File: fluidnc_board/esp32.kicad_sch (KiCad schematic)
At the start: 30 parts

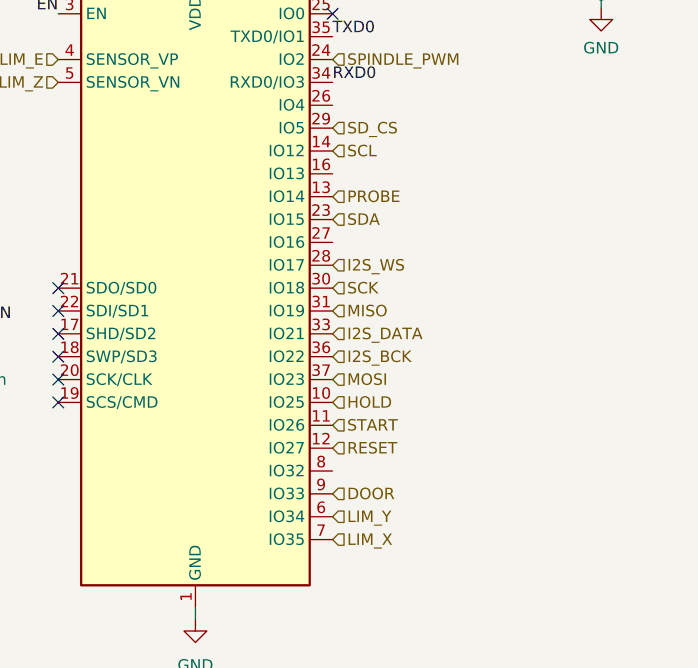
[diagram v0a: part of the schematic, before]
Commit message: outputs, spindle output and switch inputs
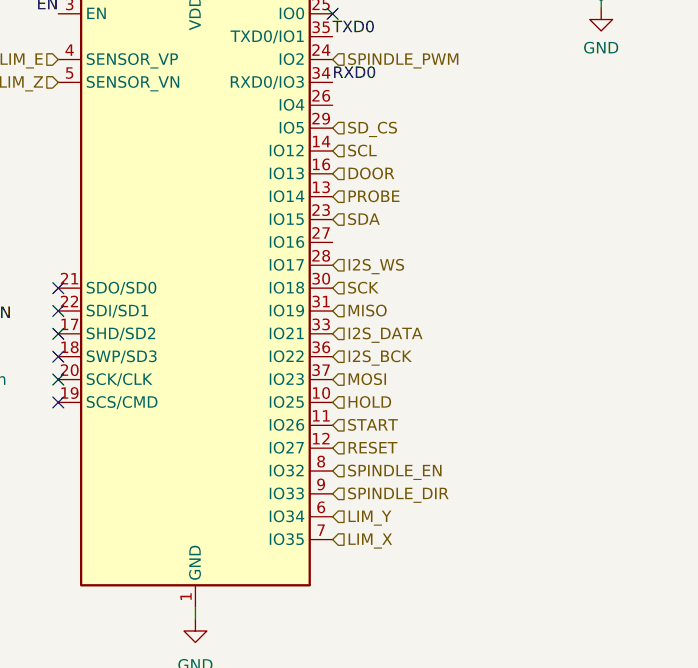
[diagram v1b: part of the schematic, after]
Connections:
- net DOOR: now also U?.16 (IO13); no longer U?.9 (IO33)
- net SPINDLE_EN: now reaches U?.8 (IO32)
- new net SPINDLE_DIR: U?.9 (IO33)
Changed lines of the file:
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@@
     (effects (font (size 1.27 1.27)) (justify left))
   )
-  (hierarchical_label "DOOR" (shape input) (at 222.25 101.6 0)
+  (hierarchical_label "DOOR" (shape input) (at 222.25 66.04 0)
     (effects (font (size 1.27 1.27)) (justify left))
   )
@@
     (effects (font (size 1.27 1.27)) (justify left))
   )
+  (hierarchical_label "SPINDLE_DIR" (shape input) (at 222.25 101.6 0)
+    (effects (font (size 1.27 1.27)) (justify left))
+  )
   (hierarchical_label "I2S_WS" (shape input) (at 222.25 76.2 0)
     (effects (font (size 1.27 1.27)) (justify left))
@@
     (effects (font (size 1.27 1.27)) (justify left))
   )
+  (hierarchical_label "SPINDLE_EN" (shape input) (at 222.25 99.06 0)
+    (effects (font (size 1.27 1.27)) (justify left))
+  )

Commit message: remove unnecessary i2s chip
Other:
- title: (none) -> ESP32 MCU
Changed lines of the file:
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@@
 (kicad_sch (version 20211123) (generator eeschema)
   (paper "A4")
+  (title_block
+    (title "ESP32 MCU")
+  )
   (junction (at 201.93 150.495) (diameter 0) (color 0 0 0 0)
   )

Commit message: footprint associations and part no.
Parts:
- C56, C58, C62: renamed from C?; footprint (none) -> Capacitor_SMD:C_0603_1608Metric_Pad1.05x0.95mm_HandSolder; Digikey Part No. (none) -> 1276-1941-1-ND
- C57: renamed from C?; footprint (none) -> Capacitor_SMD:C_0805_2012Metric_Pad1.18x1.45mm_HandSolder; Digikey Part No. (none) -> 1276-1248-1-ND
- C59, C60: renamed from C?; value C -> 100n; footprint (none) -> Capacitor_SMD:C_0603_1608Metric_Pad1.05x0.95mm_HandSolder; Digikey Part No. (none) -> 1276-1941-1-ND
- C61: renamed from C?; value 22u -> 4.7u; footprint (none) -> Capacitor_SMD:C_0805_2012Metric_Pad1.18x1.45mm_HandSolder; Digikey Part No. (none) -> 1276-1248-1-ND
- D42, D43, D44: renamed from D?; Digikey Part No. (none) -> ESD5V0D5-TPMSCT-ND
- D45, D46: renamed from D?; footprint (none) -> LED_SMD:LED_1206_3216Metric_Pad1.42x1.75mm_HandSolder; Digikey Part No. (none) -> 160-1456-1-ND
- J19: renamed from J?; footprint (none) -> Connector_USB:USB_B_OST_USB-B1HSxx_Horizontal
- Q5, Q6: renamed from Q?; Digikey Part No. (none) -> 641-1790-1-ND
- R39, R40: renamed from R?; footprint (none) -> Resistor_SMD:R_1206_3216Metric_Pad1.30x1.75mm_HandSolder; Digikey Part No. (none) -> 311-0.0ERCT-ND
- R41, R42, R49: renamed from R?; footprint (none) -> Resistor_SMD:R_0805_2012Metric_Pad1.20x1.40mm_HandSolder; Digikey Part No. (none) -> 311-10KARCT-ND
- R43, R47: renamed from R?; footprint (none) -> Resistor_SMD:R_0603_1608Metric_Pad0.98x0.95mm_HandSolder; Digikey Part No. (none) -> 311-100GRCT-ND
- R44: renamed from R?; footprint (none) -> Resistor_SMD:R_0201_0603Metric_Pad0.64x0.40mm_HandSolder; Digikey Part No. (none) -> 311-22.0KHRCT-ND
- R45: renamed from R?; footprint (none) -> Resistor_SMD:R_0805_2012Metric_Pad1.15x1.40mm_HandSolder; Digikey Part No. (none) -> 311-47KARCT-ND
- R46: renamed from R?; value R -> 2.2k; footprint (none) -> Resistor_SMD:R_0603_1608Metric_Pad0.98x0.95mm_HandSolder; Digikey Part No. (none) -> 311-2.20KHRCT-ND
- R48: renamed from R?; value R -> 10k; footprint (none) -> Resistor_SMD:R_0805_2012Metric_Pad1.20x1.40mm_HandSolder; Digikey Part No. (none) -> 311-10KARCT-ND
- SW5, SW6: renamed from SW?; footprint (none) -> Button_Switch_SMD:SW_Push_1P1T_NO_6x6mm_H9.5mm; Digikey Part No. (none) -> EG2526CT-ND
- U18: renamed from U?; Digikey Part No. (none) -> 336-5889-ND
- U19: renamed from U?; value ESP32-WROOM-32U -> ESP32-WROOM-32UE; Digikey Part No. (none) -> 1965-ESP32-WROOM-32UE(16MB)CT-ND

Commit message: fixed some footprint associations, placed footprints
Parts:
- C56, C58, C59, C60, C62: footprint Capacitor_SMD:C_0603_1608Metric_Pad1.05x0.95mm_HandSolder -> Capacitor_SMD:C_0603_1608Metric_Pad1.08x0.95mm_HandSolder; Digikey Part No. 1276-1941-1-ND -> (none)
- C57, C61: Digikey Part No. 1276-1248-1-ND -> (none)
- D42, D43, D44: Digikey Part No. ESD5V0D5-TPMSCT-ND -> (none)
- D45, D46: Digikey Part No. 160-1456-1-ND -> (none)
- Q5, Q6: Digikey Part No. 641-1790-1-ND -> (none)
- R39, R40: Digikey Part No. 311-0.0ERCT-ND -> (none)
- R41, R42, R48, R49: Digikey Part No. 311-10KARCT-ND -> (none)
- R43, R47: footprint Resistor_SMD:R_0603_1608Metric_Pad0.98x0.95mm_HandSolder -> Resistor_SMD:R_1206_3216Metric_Pad1.30x1.75mm_HandSolder; Digikey Part No. 311-100GRCT-ND -> (none)
- R44: footprint Resistor_SMD:R_0201_0603Metric_Pad0.64x0.40mm_HandSolder -> Resistor_SMD:R_0603_1608Metric_Pad0.98x0.95mm_HandSolder; Digikey Part No. 311-22.0KHRCT-ND -> (none)
- R45: footprint Resistor_SMD:R_0805_2012Metric_Pad1.15x1.40mm_HandSolder -> Resistor_SMD:R_0805_2012Metric_Pad1.20x1.40mm_HandSolder; Digikey Part No. 311-47KARCT-ND -> (none)
- R46: Digikey Part No. 311-2.20KHRCT-ND -> (none)
- SW5, SW6: Digikey Part No. EG2526CT-ND -> (none)
- U18: Digikey Part No. 336-5889-ND -> (none)
- U19: Digikey Part No. 1965-ESP32-WROOM-32UE(16MB)CT-ND -> (none)
